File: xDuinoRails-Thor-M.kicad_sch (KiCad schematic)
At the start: 1 part, among them U101 MOUDLE-SEEEDUINO-XIAO

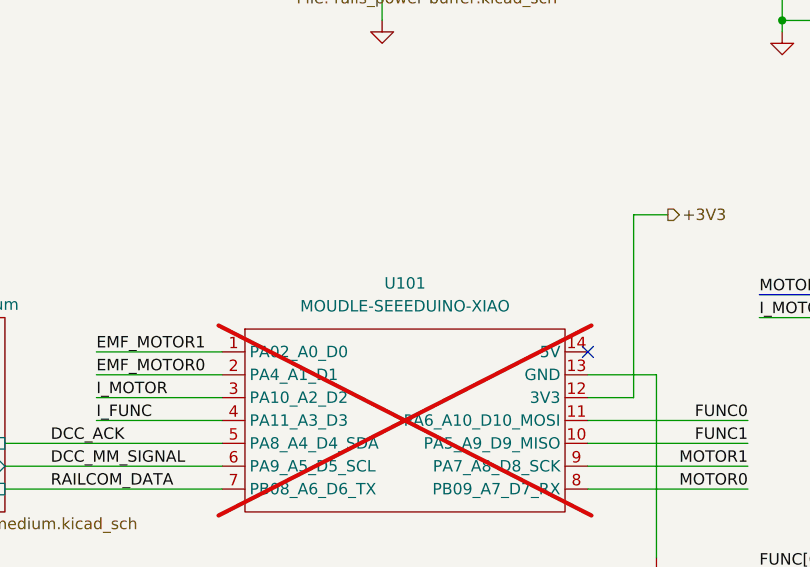
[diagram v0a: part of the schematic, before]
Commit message: Fix - revert to working model
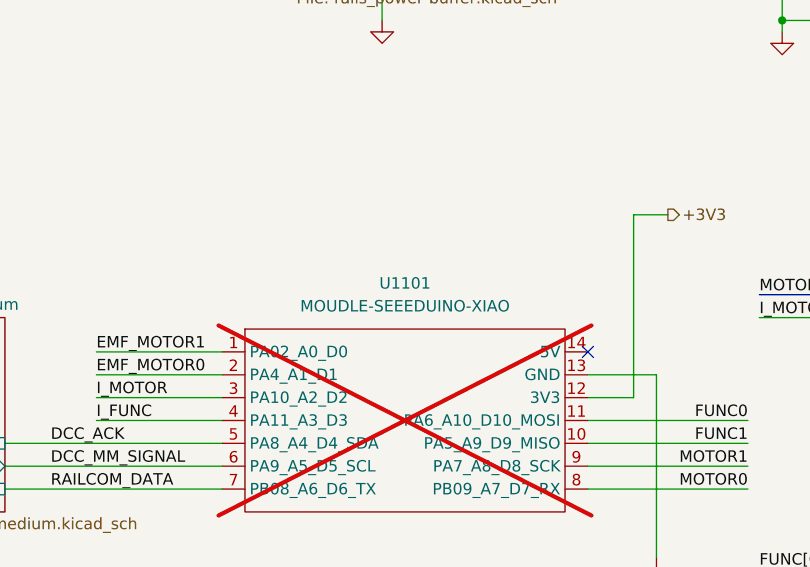
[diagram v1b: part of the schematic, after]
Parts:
- renumbered U101 to U1101
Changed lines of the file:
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@@
 		(dnp no)
 		(fields_autoplaced yes)
-		(property "Reference" "#PWR105"
+		(property "Reference" "#PWR1105"
 			(at 237.49 129.54 0)
 			(effects
@@
 			(project "xDuinoRails-Thor-M"
 				(path "/fb33ec4e-6596-45d2-a121-8d3475acd69a"
-					(reference "#PWR105")
+					(reference "#PWR1105")
 					(unit 1)
 				)
@@
 		(dnp no)
 		(fields_autoplaced yes)
-		(property "Reference" "#PWR108"
+		(property "Reference" "#PWR1108"
 			(at 171.45 149.86 0)
 			(effects
@@
 			(project "xDuinoRails-Thor-M"
 				(path "/fb33ec4e-6596-45d2-a121-8d3475acd69a"
-					(reference "#PWR108")
+					(reference "#PWR1108")
 					(unit 1)
 				)
@@
 		(dnp no)
 		(fields_autoplaced yes)
-		(property "Reference" "#PWR104"
+		(property "Reference" "#PWR1104"
 			(at 163.83 116.84 0)
 			(effects
@@
 			(project "xDuinoRails-Thor-M"
 				(path "/fb33ec4e-6596-45d2-a121-8d3475acd69a"
-					(reference "#PWR104")
+					(reference "#PWR1104")
 					(unit 1)
 				)
@@
 		(dnp no)
 		(fields_autoplaced yes)
-		(property "Reference" "#PWR102"
+		(property "Reference" "#PWR1102"
 			(at 44.45 72.39 0)
 			(effects
@@
 			(project "xDuinoRails-Hermes-M"
 				(path "/fb33ec4e-6596-45d2-a121-8d3475acd69a"
-					(reference "#PWR102")
+					(reference "#PWR1102")
 					(unit 1)
 				)
@@
 		(dnp no)
 		(fields_autoplaced yes)
-		(property "Reference" "#PWR103"
+		(property "Reference" "#PWR1103"
 			(at 144.78 72.39 0)
 			(effects
@@
 			(project "xDuinoRails-Hermes-M"
 				(path "/fb33ec4e-6596-45d2-a121-8d3475acd69a"
-					(reference "#PWR103")
+					(reference "#PWR1103")
 					(unit 1)
 				)
@@
 		(dnp no)
 		(fields_autoplaced yes)
-		(property "Reference" "#PWR106"
+		(property "Reference" "#PWR1106"
 			(at 39.37 130.81 0)
 			(effects
@@
 			(project "xDuinoRails-Hermes-M"
 				(path "/fb33ec4e-6596-45d2-a121-8d3475acd69a"
-					(reference "#PWR106")
+					(reference "#PWR1106")
 					(unit 1)
 				)
@@
 		(dnp no)
 		(fields_autoplaced yes)
-		(property "Reference" "#PWR101"
+		(property "Reference" "#PWR1101"
 			(at 100.33 71.12 0)
 			(effects
@@
 			(project "xDuinoRails-Thor-M"
 				(path "/fb33ec4e-6596-45d2-a121-8d3475acd69a"
-					(reference "#PWR101")
+					(reference "#PWR1101")
 					(unit 1)
 				)
@@
 		(dnp yes)
 		(fields_autoplaced yes)
-		(property "Reference" "U101"
+		(property "Reference" "U1101"
 			(at 102.87 93.98 0)
 			(effects
@@
 			(project ""
 				(path "/fb33ec4e-6596-45d2-a121-8d3475acd69a"
-					(reference "U101")
+					(reference "U1101")
 					(unit 1)
 				)
@@
 		(dnp no)
 		(fields_autoplaced yes)
-		(property "Reference" "#PWR107"
+		(property "Reference" "#PWR1107"
 			(at 130.81 130.81 0)
 			(effects
@@
 			(project "xDuinoRails-Hermes-S"
 				(path "/fb33ec4e-6596-45d2-a121-8d3475acd69a"
-					(reference "#PWR107")
+					(reference "#PWR1107")
 					(unit 1)
 				)
@@
 		)
 	)
-	(sheet_instances
-		(path "/"
-			(page "1")
-		)
-	)

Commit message: Fix - Remove ERC error, refresh annotation
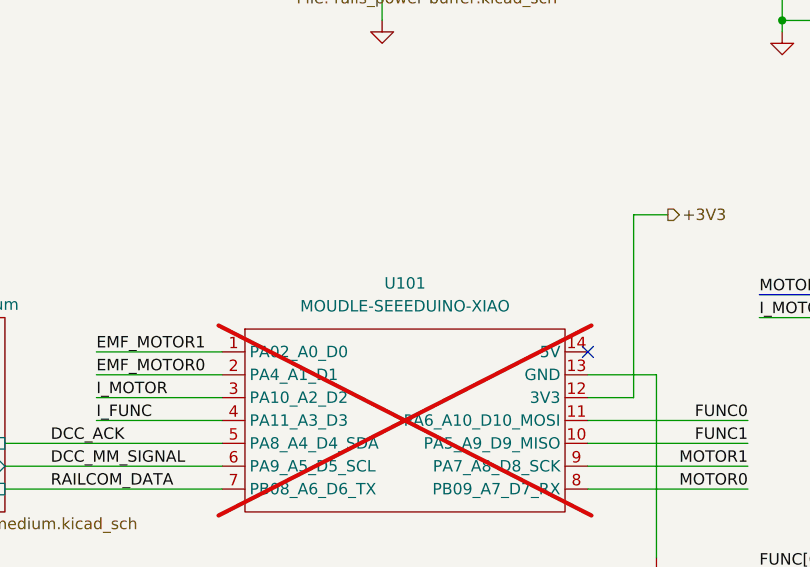
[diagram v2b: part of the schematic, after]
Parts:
- renumbered U1101 to U101
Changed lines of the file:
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@@
 		(dnp no)
 		(fields_autoplaced yes)
-		(property "Reference" "#PWR1105"
+		(property "Reference" "#PWR105"
 			(at 237.49 129.54 0)
 			(effects
@@
 			(project "xDuinoRails-Thor-M"
 				(path "/fb33ec4e-6596-45d2-a121-8d3475acd69a"
-					(reference "#PWR1105")
+					(reference "#PWR105")
 					(unit 1)
 				)
@@
 		(dnp no)
 		(fields_autoplaced yes)
-		(property "Reference" "#PWR1108"
+		(property "Reference" "#PWR108"
 			(at 171.45 149.86 0)
 			(effects
@@
 			(project "xDuinoRails-Thor-M"
 				(path "/fb33ec4e-6596-45d2-a121-8d3475acd69a"
-					(reference "#PWR1108")
+					(reference "#PWR108")
 					(unit 1)
 				)
@@
 		(dnp no)
 		(fields_autoplaced yes)
-		(property "Reference" "#PWR1104"
+		(property "Reference" "#PWR104"
 			(at 163.83 116.84 0)
 			(effects
@@
 			(project "xDuinoRails-Thor-M"
 				(path "/fb33ec4e-6596-45d2-a121-8d3475acd69a"
-					(reference "#PWR1104")
+					(reference "#PWR104")
 					(unit 1)
 				)
@@
 		(dnp no)
 		(fields_autoplaced yes)
-		(property "Reference" "#PWR1102"
+		(property "Reference" "#PWR102"
 			(at 44.45 72.39 0)
 			(effects
@@
 			(project "xDuinoRails-Hermes-M"
 				(path "/fb33ec4e-6596-45d2-a121-8d3475acd69a"
-					(reference "#PWR1102")
+					(reference "#PWR102")
 					(unit 1)
 				)
@@
 		(dnp no)
 		(fields_autoplaced yes)
-		(property "Reference" "#PWR1103"
+		(property "Reference" "#PWR103"
 			(at 144.78 72.39 0)
 			(effects
@@
 			(project "xDuinoRails-Hermes-M"
 				(path "/fb33ec4e-6596-45d2-a121-8d3475acd69a"
-					(reference "#PWR1103")
+					(reference "#PWR103")
 					(unit 1)
 				)
@@
 		(dnp no)
 		(fields_autoplaced yes)
-		(property "Reference" "#PWR1106"
+		(property "Reference" "#PWR106"
 			(at 39.37 130.81 0)
 			(effects
@@
 			(project "xDuinoRails-Hermes-M"
 				(path "/fb33ec4e-6596-45d2-a121-8d3475acd69a"
-					(reference "#PWR1106")
+					(reference "#PWR106")
 					(unit 1)
 				)
@@
 		(dnp no)
 		(fields_autoplaced yes)
-		(property "Reference" "#PWR1101"
+		(property "Reference" "#PWR101"
 			(at 100.33 71.12 0)
 			(effects
@@
 			(project "xDuinoRails-Thor-M"
 				(path "/fb33ec4e-6596-45d2-a121-8d3475acd69a"
-					(reference "#PWR1101")
+					(reference "#PWR101")
 					(unit 1)
 				)
@@
 		(dnp yes)
 		(fields_autoplaced yes)
-		(property "Reference" "U1101"
+		(property "Reference" "U101"
 			(at 102.87 93.98 0)
 			(effects
@@
 			(project ""
 				(path "/fb33ec4e-6596-45d2-a121-8d3475acd69a"
-					(reference "U1101")
+					(reference "U101")
 					(unit 1)
 				)
@@
 		(dnp no)
 		(fields_autoplaced yes)
-		(property "Reference" "#PWR1107"
+		(property "Reference" "#PWR107"
 			(at 130.81 130.81 0)
 			(effects
@@
 			(project "xDuinoRails-Hermes-S"
 				(path "/fb33ec4e-6596-45d2-a121-8d3475acd69a"
-					(reference "#PWR1107")
+					(reference "#PWR107")
 					(unit 1)
 				)
@@
 		)
 	)
+	(sheet_instances
+		(path "/"
+			(page "1")
+		)
+	)
